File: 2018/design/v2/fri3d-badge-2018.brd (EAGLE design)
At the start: 80 x 60 mm, 136 parts

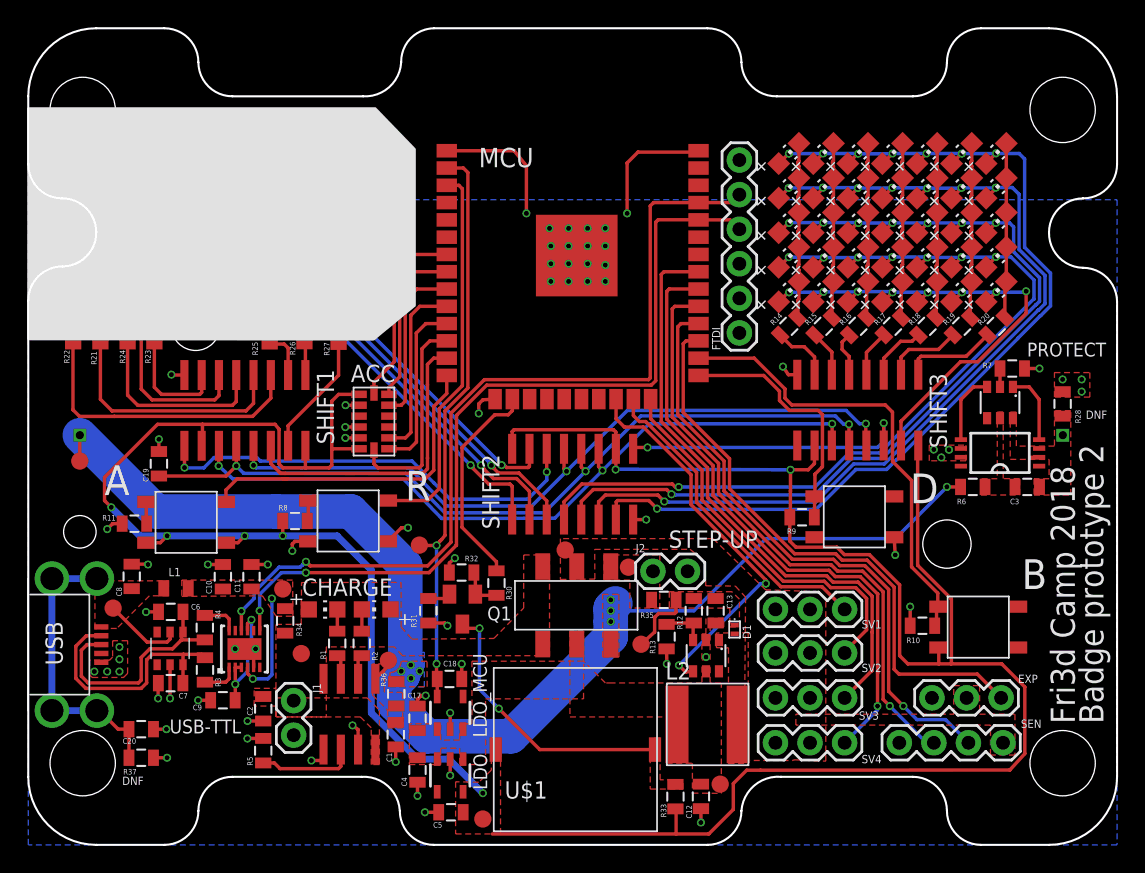
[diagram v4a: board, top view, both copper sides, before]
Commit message: added 3 missing traces/connections to ESP
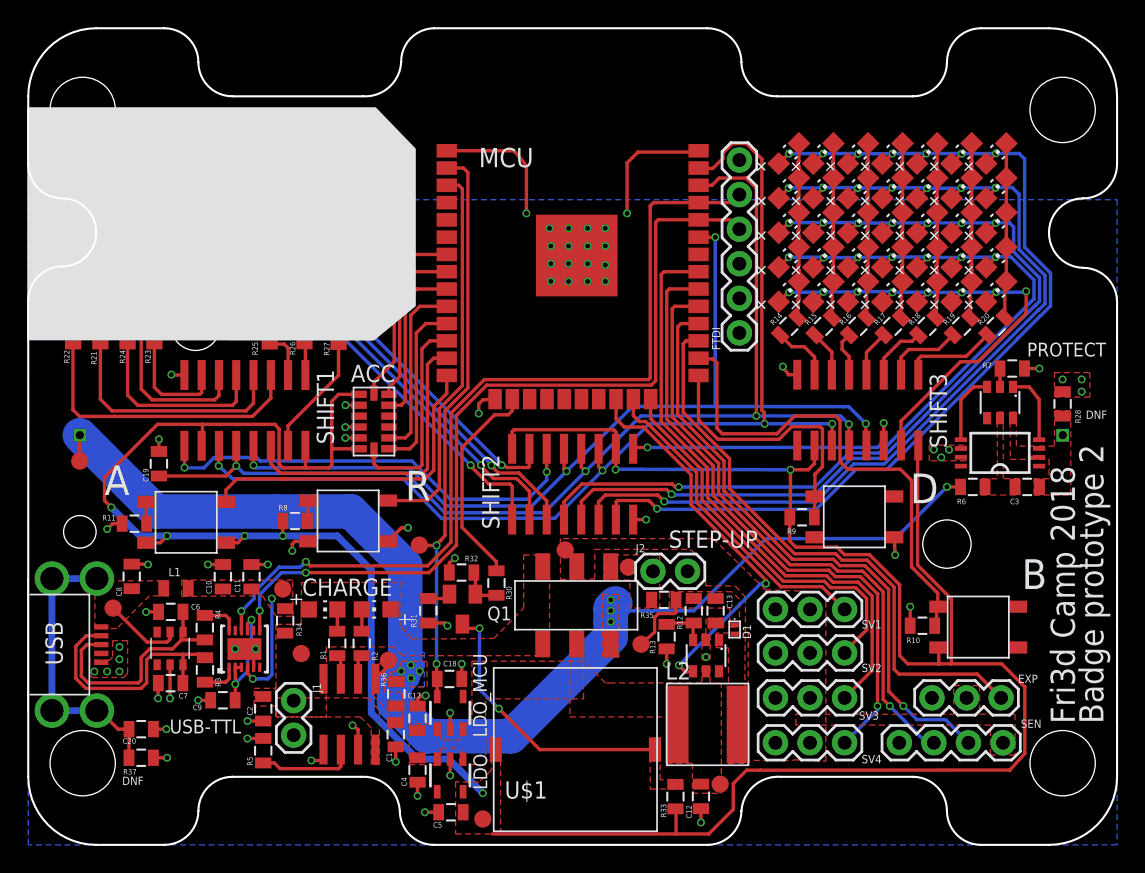
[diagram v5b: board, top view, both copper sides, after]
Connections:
- net LEDS_ENABLE: now also MCU.33
- net LEDS_RCK: now also MCU.36
- net LEDS_SCK: now also MCU.37
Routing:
- net LEDS_SCK: track 54.4 -> 80.0 mm, vias 3 -> 4
- net LEDS_RCK: track 60.6 -> 82.1 mm, vias 3 -> 4
- net LEDS_ENABLE: track 54.4 -> 68.4 mm, vias 3 -> 4
- net BUTTON-A: track 33.8 -> 36.9 mm
- net DOWNLOAD: track 18.5 -> 20.1 mm
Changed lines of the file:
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@@
 <wire x1="57.755" y1="24.07" x2="57.775" y2="24.775" width="0.254" layer="1"/>
 <wire x1="57.775" y1="24.775" x2="57.775" y2="25.6" width="0.254" layer="1"/>
-<wire x1="55.196" y1="32.645" x2="55.196" y2="33.33265625" width="0.254" layer="1"/>
-<wire x1="55.196" y1="33.33265625" x2="54.03865625" y2="34.49" width="0.254" layer="1"/>
-<wire x1="54.03865625" y1="34.49" x2="49.25" y2="34.49" width="0.254" layer="1"/>
 <wire x1="57.775" y1="25.6" x2="57.8" y2="25.625" width="0.254" layer="1"/>
-<wire x1="58.352" y1="31.602" x2="58.36" y2="31.61" width="0.254" layer="1"/>
 <wire x1="57.8" y1="27.22865625" x2="58.352" y2="27.78065625" width="0.254" layer="1"/>
-<wire x1="58.352" y1="27.78065625" x2="58.352" y2="31.602" width="0.254" layer="1"/>
 <wire x1="57.8" y1="25.625" x2="57.8" y2="27.22865625" width="0.254" layer="1"/>
-<wire x1="58.36" y1="31.61" x2="58.05" y2="31.92" width="0.254" layer="1"/>
-<wire x1="58.05" y1="31.92" x2="55.93265625" y2="31.92" width="0.254" layer="1"/>
-<wire x1="55.20765625" y1="32.645" x2="55.196" y2="32.645" width="0.254" layer="1"/>
-<wire x1="55.93265625" y1="31.92" x2="55.20765625" y2="32.645" width="0.254" layer="1"/>
+<wire x1="58.352" y1="30.5577375" x2="58.1897375" y2="30.72" width="0.254" layer="1"/>
+<wire x1="55.1702625" y1="29.8" x2="50.67075" y2="29.8" width="0.254" layer="1"/>
+<wire x1="56.0902625" y1="30.72" x2="55.1702625" y2="29.8" width="0.254" layer="1"/>
+<wire x1="58.352" y1="27.78065625" x2="58.352" y2="30.5577375" width="0.254" layer="1"/>
+<wire x1="58.1897375" y1="30.72" x2="56.0902625" y2="30.72" width="0.254" layer="1"/>
+<wire x1="49.25" y1="31.22075" x2="49.25" y2="34.49" width="0.254" layer="1"/>
+<wire x1="50.67075" y1="29.8" x2="49.25" y2="31.22075" width="0.254" layer="1"/>
 </signal>
 <signal name="BUTTON-A">
@@
 <contactref element="R10" pad="2"/>
 <wire x1="66.875" y1="17.5" x2="66.7375" y2="17.6375" width="0.254" layer="1"/>
-<wire x1="63.548" y1="28.1282625" x2="63.548" y2="28.152" width="0.254" layer="1"/>
-<wire x1="63.548" y1="28.152" x2="63.5" y2="28.2" width="0.254" layer="1"/>
-<wire x1="63.548" y1="28.1282625" x2="64.9" y2="26.7762625" width="0.254" layer="1"/>
-<wire x1="63.5" y1="28.2" x2="63.5" y2="31.8" width="0.254" layer="1"/>
-<wire x1="62.976" y1="32.324" x2="56.1" y2="32.324" width="0.254" layer="1"/>
-<wire x1="63.5" y1="31.8" x2="62.976" y2="32.324" width="0.254" layer="1"/>
-<wire x1="56.1" y1="32.324" x2="55.6" y2="32.824" width="0.254" layer="1"/>
-<wire x1="55.6" y1="32.824" x2="55.6" y2="33.5" width="0.254" layer="1"/>
 <wire x1="66.6" y1="16.1" x2="66.7375" y2="16.2375" width="0.254" layer="1"/>
 <wire x1="66.7375" y1="16.2375" x2="66.7375" y2="17.6375" width="0.254" layer="1"/>
@@
 <wire x1="66.827696875" y1="18.492696875" x2="66.827696875" y2="17.547303125" width="0.254" layer="1"/>
 <wire x1="66.827696875" y1="17.547303125" x2="66.875" y2="17.5" width="0.254" layer="1"/>
-<wire x1="64.9" y1="26.7762625" x2="64.9" y2="20.42039375" width="0.254" layer="1"/>
+<wire x1="64.9" y1="20.42039375" x2="64.9" y2="26.7762625" width="0.254" layer="1"/>
 <contactref element="MCU" pad="26"/>
-<wire x1="53.34" y1="35.76" x2="49.25" y2="35.76" width="0.254" layer="1"/>
-<wire x1="55.6" y1="33.5" x2="53.34" y2="35.76" width="0.254" layer="1"/>
+<wire x1="64.9" y1="26.7762625" x2="64.0762625" y2="27.6" width="0.254" layer="1"/>
+<wire x1="64.0762625" y1="27.6" x2="60.2" y2="27.6" width="0.254" layer="1"/>
+<wire x1="59.642" y1="31.17900625" x2="59.30400625" y2="31.517" width="0.254" layer="1"/>
+<wire x1="60.2" y1="27.6" x2="59.642" y2="28.158" width="0.254" layer="1"/>
+<wire x1="59.642" y1="28.158" x2="59.642" y2="31.17900625" width="0.254" layer="1"/>
+<wire x1="59.30400625" y1="31.517" x2="56.31591875" y2="31.517" width="0.254" layer="1"/>
+<wire x1="56.31591875" y1="31.517" x2="55.00291875" y2="30.204" width="0.254" layer="1"/>
+<wire x1="50.996" y1="30.204" x2="50.6" y2="30.6" width="0.254" layer="1"/>
+<wire x1="50.6" y1="30.6" x2="50.6" y2="35.4" width="0.254" layer="1"/>
+<wire x1="50.6" y1="35.4" x2="50.3" y2="35.7" width="0.254" layer="1"/>
+<wire x1="50.3" y1="35.7" x2="49.31" y2="35.7" width="0.254" layer="1"/>
+<wire x1="49.31" y1="35.7" x2="49.25" y2="35.76" width="0.254" layer="1"/>
+<wire x1="55.00291875" y1="30.204" x2="50.996" y2="30.204" width="0.254" layer="1"/>
 </signal>
 <signal name="BUTTON-B">
@@
 <wire x1="59.06" y1="29.328" x2="59.045" y2="29.343" width="0.254" layer="1"/>
 <wire x1="42.192" y1="27.508" x2="45.624" y2="30.94" width="0.254" layer="16"/>
-<wire x1="45.624" y1="30.94" x2="59.065" y2="30.94" width="0.254" layer="16"/>
+<wire x1="45.624" y1="30.94" x2="54.1" y2="30.94" width="0.254" layer="16"/>
 <via x="59.065" y="30.94" extent="1-16" drill="0.35"/>
+<wire x1="54.1" y1="30.94" x2="59.065" y2="30.94" width="0.254" layer="16"/>
 <wire x1="59.065" y1="30.94" x2="59.065" y2="29.363" width="0.254" layer="1"/>
 <wire x1="59.065" y1="29.363" x2="59.045" y2="29.343" width="0.254" layer="1"/>
+<contactref element="MCU" pad="37"/>
+<via x="54.1" y="30.94" extent="1-16" drill="0.35"/>
+<wire x1="51.74598125" y1="51.5328" x2="52.75401875" y2="51.5328" width="0.254" layer="1"/>
+<wire x1="53.904" y1="31.92900625" x2="54.077" y2="31.75600625" width="0.254" layer="1"/>
+<wire x1="54.077" y1="30.963" x2="54.1" y2="30.94" width="0.254" layer="1"/>
+<wire x1="54.077" y1="31.75600625" x2="54.077" y2="30.963" width="0.254" layer="1"/>
+<wire x1="52.75401875" y1="51.5328" x2="53.904" y2="50.38281875" width="0.254" layer="1"/>
+<wire x1="53.904" y1="50.38281875" x2="53.904" y2="31.92900625" width="0.254" layer="1"/>
+<wire x1="49.25" y1="49.73" x2="49.28" y2="49.7" width="0.254" layer="1"/>
+<wire x1="49.28" y1="49.7" x2="50.3" y2="49.7" width="0.254" layer="1"/>
+<wire x1="50.3" y1="49.7" x2="51.0332" y2="50.4332" width="0.254" layer="1"/>
+<wire x1="51.0332" y1="50.4332" x2="51.0332" y2="50.82001875" width="0.254" layer="1"/>
+<wire x1="51.0332" y1="50.82001875" x2="51.74598125" y2="51.5328" width="0.254" layer="1"/>
 </signal>
 <signal name="LEDS_RCK">
@@
 <wire x1="30.596" y1="24.404" x2="27.76" y2="27.29" width="0.254" layer="16"/>
 <via x="60.3" y="30.9" extent="1-16" drill="0.35"/>
-<wire x1="59.92100625" y1="30.9" x2="60.3" y2="30.9" width="0.254" layer="16"/>
-<wire x1="59.30400625" y1="31.517" x2="59.92100625" y2="30.9" width="0.254" layer="16"/>
-<wire x1="40.95" y1="27.45" x2="45.017" y2="31.517" width="0.254" layer="16"/>
-<wire x1="45.017" y1="31.517" x2="59.30400625" y2="31.517" width="0.254" layer="16"/>
+<wire x1="45.017" y1="31.517" x2="40.95" y2="27.45" width="0.254" layer="16"/>
 <wire x1="60.3" y1="30.9" x2="60.3" y2="29.358" width="0.254" layer="1"/>
 <wire x1="60.3" y1="29.358" x2="60.315" y2="29.343" width="0.254" layer="1"/>
@@
 <wire x1="15.285" y1="27.845" x2="14.54" y2="27.1" width="0.254" layer="1"/>
 <wire x1="14.54" y1="27.1" x2="9.6" y2="27.1" width="0.254" layer="1"/>
+<contactref element="MCU" pad="36"/>
+<wire x1="60.3" y1="30.9" x2="59.683" y2="31.517" width="0.254" layer="16"/>
+<wire x1="59.683" y1="31.517" x2="53.5" y2="31.517" width="0.254" layer="16"/>
+<wire x1="53.5" y1="31.517" x2="45.017" y2="31.517" width="0.254" layer="16"/>
+<via x="53.5" y="31.517" extent="1-16" drill="0.35"/>
+<wire x1="50.7688" y1="48.9928" x2="52.75401875" y2="48.9928" width="0.254" layer="1"/>
+<wire x1="49.25" y1="48.46" x2="50.236" y2="48.46" width="0.254" layer="1"/>
+<wire x1="50.236" y1="48.46" x2="50.7688" y2="48.9928" width="0.254" layer="1"/>
+<wire x1="52.75401875" y1="48.9928" x2="53.5" y2="48.24681875" width="0.254" layer="1"/>
+<wire x1="53.5" y1="48.24681875" x2="53.5" y2="31.517" width="0.254" layer="1"/>
 </signal>
 <signal name="VUSB">
@@
 <wire x1="28" y1="27.7" x2="27.87134375" y2="27.7" width="0.254" layer="16"/>
 <wire x1="27.87134375" y1="27.7" x2="27.86734375" y2="27.704" width="0.254" layer="16"/>
-<wire x1="27.86734375" y1="27.704" x2="20.1" y2="27.704" width="0.254" layer="16"/>
-<wire x1="20.1" y1="27.704" x2="16.731" y2="27.704" width="0.254" layer="16"/>
+<wire x1="27.86734375" y1="27.704" x2="16.731" y2="27.704" width="0.254" layer="16"/>
 <wire x1="16.731" y1="27.704" x2="16.55" y2="27.885" width="0.254" layer="16"/>
 <via x="61.54" y="30.945" extent="1-16" drill="0.35"/>
-<wire x1="61.07100625" y1="30.945" x2="61.54" y2="30.945" width="0.254" layer="16"/>
-<wire x1="39.55" y1="27.45" x2="44.021" y2="31.921" width="0.254" layer="16"/>
-<wire x1="44.021" y1="31.921" x2="60.09500625" y2="31.921" width="0.254" layer="16"/>
-<wire x1="60.09500625" y1="31.921" x2="61.07100625" y2="30.945" width="0.254" layer="16"/>
+<wire x1="39.55" y1="27.45" x2="44.421" y2="32.221" width="0.254" layer="16"/>
+<wire x1="59.879" y1="32.19500625" x2="50.70001875" y2="32.210440625" width="0.254" layer="16"/>
+<wire x1="50.70001875" y1="32.210440625" x2="44.421" y2="32.221" width="0.254" layer="16"/>
 <wire x1="61.54" y1="30.945" x2="61.54" y2="29.388" width="0.254" layer="1"/>
 <wire x1="61.54" y1="29.388" x2="61.585" y2="29.343" width="0.254" layer="1"/>
+<contactref element="MCU" pad="33"/>
+<wire x1="61.54" y1="30.945" x2="60.28999375" y2="32.19500625" width="0.254" layer="16"/>
+<wire x1="60.28999375" y1="32.19500625" x2="59.879" y2="32.19500625" width="0.254" layer="16"/>
+<wire x1="50.70001875" y1="32.210440625" x2="50.48" y2="32.430459375" width="0.254" layer="16"/>
+<wire x1="50.48" y1="32.430459375" x2="50.48" y2="44.645" width="0.254" layer="16"/>
+<via x="50.48" y="44.645" extent="1-16" drill="0.35"/>
+<wire x1="50.48" y1="44.645" x2="49.255" y2="44.645" width="0.254" layer="1"/>
+<wire x1="49.255" y1="44.645" x2="49.25" y2="44.65" width="0.254" layer="1"/>
 </signal>
 <signal name="VSTEPUP">

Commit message: several bugfixes in schema and layout
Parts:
- removed C19: 1uF, passive:0805
- removed EXP: (no value), SparkFun-Connectors:1X03
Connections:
- removed net 5V_ENABLE: MCU.22, STEP-UP.4
- removed net EXP_IO: EXP.3, MCU.27
- net 5V: no longer EXP.2
- net ACC_SCK: now also MCU.27; no longer MCU.7
- net GND: no longer C19.1, EXP.1
- net LEDS_RCK: no longer C19.2
- net VCC: now also STEP-UP.4
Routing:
- net EXP_IO: track 43.1 -> 0.00 mm
- net 5V_ENABLE: track 29.1 -> 0.00 mm, vias 2 -> 0
- net ACC_SCK: track 14.2 -> 35.2 mm, vias 0 -> 2
- net LEDS_RCK: track 82.1 -> 76.1 mm
- net GND: track 73.2 -> 72.3 mm, vias 70 -> 69
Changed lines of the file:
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@@
 <attribute name="VALUE" x="62.73" y="5.468" size="0.6096" layer="27" font="vector" ratio="20"/>
-</element>
-<element name="EXP" library="SparkFun-Connectors" library_urn="urn:adsk.eagle:library:513" package="1X03" package3d_urn="urn:adsk.eagle:package:38063/1" value="" x="66.4" y="10.8" smashed="yes">
-<attribute name="NAME" x="72.73" y="11.897" size="0.6096" layer="25" font="vector" ratio="20"/>
-<attribute name="VALUE" x="65.13" y="8.768" size="0.6096" layer="27" font="vector" ratio="20"/>
 </element>
 <element name="LDO_MCU" library="power" package="SOT23-5" value="XC6210" x="31" y="9.7" smashed="yes">
@@
 <attribute name="NAME" x="30.488" y="13.1155" size="0.4064" layer="25"/>
 <attribute name="VALUE" x="30.534" y="10.893" size="0.4064" layer="27"/>
-</element>
-<element name="C19" library="passive" package="0805" value="1uF" x="9.6" y="28" smashed="yes" rot="R270">
-<attribute name="NAME" x="8.4255" y="27.662" size="0.4064" layer="25" rot="R270"/>
-<attribute name="VALUE" x="8.503" y="29.416" size="0.4064" layer="27" rot="R270"/>
 </element>
 <element name="U$1" library="sound" package="KLJ-1230" value="KLJ-1230" x="40.2" y="7" smashed="yes">
@@
 <contactref element="SV4" pad="1"/>
 <contactref element="SEN" pad="1"/>
-<contactref element="EXP" pad="1"/>
 <polygon width="0.1524" layer="16" thermals="no" rank="2">
 <vertex x="0.1" y="47.4"/>
@@
 <wire x1="33.1" y1="32.4" x2="33.1" y2="31.7" width="0.254" layer="1"/>
 <via x="33.1" y="31.7" extent="1-16" drill="0.35"/>
-<contactref element="C19" pad="1"/>
 <wire x1="56.505" y1="34.543" x2="55.853" y2="34.543" width="0.254" layer="1"/>
 <wire x1="55.853" y1="34.543" x2="55.45" y2="35.14" width="0.254" layer="1"/>
@@
 <wire x1="16.4" y1="20.6" x2="17.6" y2="20.6" width="0.254" layer="1"/>
 <via x="17.6" y="20.6" extent="1-16" drill="0.35"/>
-<wire x1="9.6" y1="28.9" x2="9.6" y2="29.8" width="0.254" layer="1"/>
-<via x="9.6" y="29.8" extent="1-16" drill="0.35"/>
 <wire x1="17.265" y1="7.82" x2="16.11" y2="7.82" width="0.254" layer="1"/>
 <wire x1="16.11" y1="7.82" x2="16.1" y2="7.81" width="0.254" layer="1"/>
@@
 <vertex x="50.1" y="11.91"/>
 <vertex x="50.1" y="13.1"/>
-<vertex x="49.5" y="13.1"/>
-<vertex x="49.5" y="11.9"/>
+<vertex x="48.6" y="13.1"/>
+<vertex x="48.6" y="11.9"/>
 <vertex x="42.91" y="11.895"/>
 <vertex x="42.405" y="11.895"/>
@@
 <vertex x="30.3" y="8.9"/>
 </polygon>
+<contactref element="STEP-UP" pad="4"/>
 </signal>
 <signal name="RESET">
@@
 <contactref element="SV4" pad="2"/>
 <contactref element="SEN" pad="4"/>
-<contactref element="EXP" pad="2"/>
 <wire x1="57.44" y1="17.3" x2="57.44" y2="16.9" width="0.254" layer="1"/>
 <contactref element="TP11" pad="TP"/>
@@
 <vertex x="56.4" y="9.6"/>
 <vertex x="68" y="9.6"/>
-<vertex x="68" y="11.7"/>
-<vertex x="69.9" y="11.7"/>
 <vertex x="69.9" y="9.6"/>
 <vertex x="72.5" y="9.6"/>
@@
 <vertex x="52.9" y="15.585"/>
 </polygon>
-</signal>
-<signal name="5V_ENABLE">
-<contactref element="STEP-UP" pad="4"/>
-<wire x1="54.19503125" y1="19.29503125" x2="54.195825" y2="19.19503125" width="0.254" layer="16"/>
-<via x="54.195825" y="19.19503125" extent="1-16" drill="0.35"/>
-<contactref element="MCU" pad="22"/>
-<wire x1="54.195825" y1="19.19503125" x2="54.200825" y2="19.449175" width="0.254" layer="1"/>
-<wire x1="48.7" y1="25" x2="48.7" y2="27.2" width="0.254" layer="1"/>
-<wire x1="48.7" y1="27.2" x2="45.2" y2="30.7" width="0.254" layer="1"/>
-<wire x1="45.2" y1="30.7" x2="43.8" y2="30.7" width="0.254" layer="1"/>
-<wire x1="43.8" y1="30.7" x2="43.19" y2="31.31" width="0.254" layer="1"/>
-<wire x1="43.19" y1="31.31" x2="43.19" y2="32.75" width="0.254" layer="1"/>
-<wire x1="54.200825" y1="19.449175" x2="48.7" y2="25" width="0.254" layer="1"/>
-<wire x1="48.85" y1="12.75" x2="48.3" y2="12.7" width="0.254" layer="1"/>
-<wire x1="48.3" y1="12.7" x2="47.808003125" y2="13.191996875" width="0.254" layer="1"/>
-<via x="47.808003125" y="13.191996875" extent="1-16" drill="0.35"/>
-<wire x1="47.808003125" y1="13.191996875" x2="53.8110375" y2="19.19503125" width="0.254" layer="16"/>
-<wire x1="53.8110375" y1="19.19503125" x2="54.195825" y2="19.19503125" width="0.254" layer="16"/>
 </signal>
 <signal name="N$18">
@@
 <contactref element="SHIFT1" pad="12"/>
 <contactref element="SHIFT2" pad="12"/>
-<contactref element="C19" pad="2"/>
 <wire x1="40.635" y1="29.1" x2="40.635" y2="27.765" width="0.254" layer="1"/>
 <wire x1="40.635" y1="27.765" x2="40.95" y2="27.45" width="0.254" layer="1"/>
@@
 <wire x1="60.3" y1="29.358" x2="60.315" y2="29.343" width="0.254" layer="1"/>
 <wire x1="15.285" y1="27.685" x2="15.285" y2="27.845" width="0.254" layer="1"/>
-<wire x1="15.285" y1="27.845" x2="14.54" y2="27.1" width="0.254" layer="1"/>
-<wire x1="14.54" y1="27.1" x2="9.6" y2="27.1" width="0.254" layer="1"/>
 <contactref element="MCU" pad="36"/>
 <wire x1="60.3" y1="30.9" x2="59.683" y2="31.517" width="0.254" layer="16"/>
@@
 <signal name="ACC_SCK">
 <contactref element="ACC" pad="14"/>
-<contactref element="MCU" pad="7"/>
-<wire x1="25.4025" y1="33.2" x2="25.4025" y2="34.0025" width="0.254" layer="1"/>
-<wire x1="26.888" y1="35.488" x2="26.888" y2="40.3306875" width="0.254" layer="1"/>
-<wire x1="26.888" y1="40.3306875" x2="26.89" y2="40.3326875" width="0.254" layer="1"/>
-<wire x1="26.89" y1="40.3326875" x2="26.89" y2="42.53" width="0.254" layer="1"/>
-<wire x1="25.4025" y1="34.0025" x2="26.888" y2="35.488" width="0.254" layer="1"/>
-<wire x1="26.89" y1="42.53" x2="27.74" y2="43.38" width="0.254" layer="1"/>
-<wire x1="27.74" y1="43.38" x2="30.75" y2="43.38" width="0.254" layer="1"/>
+<contactref element="MCU" pad="27"/>
+<wire x1="25.4025" y1="33.2" x2="25.6505" y2="33.448" width="0.254" layer="1"/>
+<wire x1="25.6505" y1="33.448" x2="25.6505" y2="33.4922375" width="0.254" layer="1"/>
+<wire x1="25.6505" y1="33.4922375" x2="26.888" y2="34.7297375" width="0.254" layer="1"/>
+<wire x1="26.888" y1="42.288" x2="28" y2="43.4" width="0.254" layer="1"/>
+<wire x1="28" y1="43.4" x2="28.7" y2="43.4" width="0.254" layer="1"/>
+<via x="28.7" y="43.4" extent="1-16" drill="0.35"/>
+<wire x1="28.7" y1="43.4" x2="32.7" y2="43.4" width="0.254" layer="16"/>
+<wire x1="32.7" y1="43.4" x2="39.1" y2="37" width="0.254" layer="16"/>
+<wire x1="39.1" y1="37" x2="48.296" y2="37" width="0.254" layer="16"/>
+<via x="48.296" y="37" extent="1-16" drill="0.35"/>
+<wire x1="48.296" y1="37" x2="49.22" y2="37" width="0.254" layer="1"/>
+<wire x1="49.22" y1="37" x2="49.25" y2="37.03" width="0.254" layer="1"/>
+<wire x1="26.888" y1="34.7297375" x2="26.888" y2="42.288" width="0.254" layer="1"/>
 </signal>
 <signal name="SERVO1">
@@
 <wire x1="69.08" y1="7.52" x2="69.08" y2="7.5" width="0.254" layer="16"/>
 </signal>
-<signal name="EXP_IO">
-<contactref element="EXP" pad="3"/>
-<contactref element="MCU" pad="27"/>
-<wire x1="51.528" y1="28.37140625" x2="51.528" y2="26.17140625" width="0.254" layer="1"/>
-<wire x1="51.528" y1="28.37140625" x2="48.123" y2="31.77640625" width="0.254" layer="1"/>
-<wire x1="56.31040625" y1="21.389" x2="59.3290625" y2="21.389" width="0.254" layer="1"/>
-<wire x1="59.3290625" y1="21.389" x2="59.7980625" y2="20.92" width="0.254" layer="1"/>
-<wire x1="51.528" y1="26.17140625" x2="56.31040625" y2="21.389" width="0.254" layer="1"/>
-<wire x1="61.63671875" y1="20.92" x2="63.622" y2="18.93471875" width="0.254" layer="1"/>
-<wire x1="63.622" y1="18.93471875" x2="63.622" y2="12.9" width="0.254" layer="1"/>
-<wire x1="59.7980625" y1="20.92" x2="61.63671875" y2="20.92" width="0.254" layer="1"/>
-<wire x1="63.622" y1="12.9" x2="63.977" y2="12.545" width="0.254" layer="1"/>
-<wire x1="69.735" y1="12.545" x2="71.48" y2="10.8" width="0.254" layer="1"/>
-<wire x1="63.977" y1="12.545" x2="69.735" y2="12.545" width="0.254" layer="1"/>
-<wire x1="48.33" y1="37.03" x2="49.25" y2="37.03" width="0.254" layer="1"/>
-<wire x1="48.123" y1="31.77640625" x2="48.123" y2="36.823" width="0.254" layer="1"/>
-<wire x1="48.123" y1="36.823" x2="48.33" y2="37.03" width="0.254" layer="1"/>
-</signal>
 <signal name="N$62">
